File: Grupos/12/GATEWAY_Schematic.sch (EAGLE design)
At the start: 13 parts

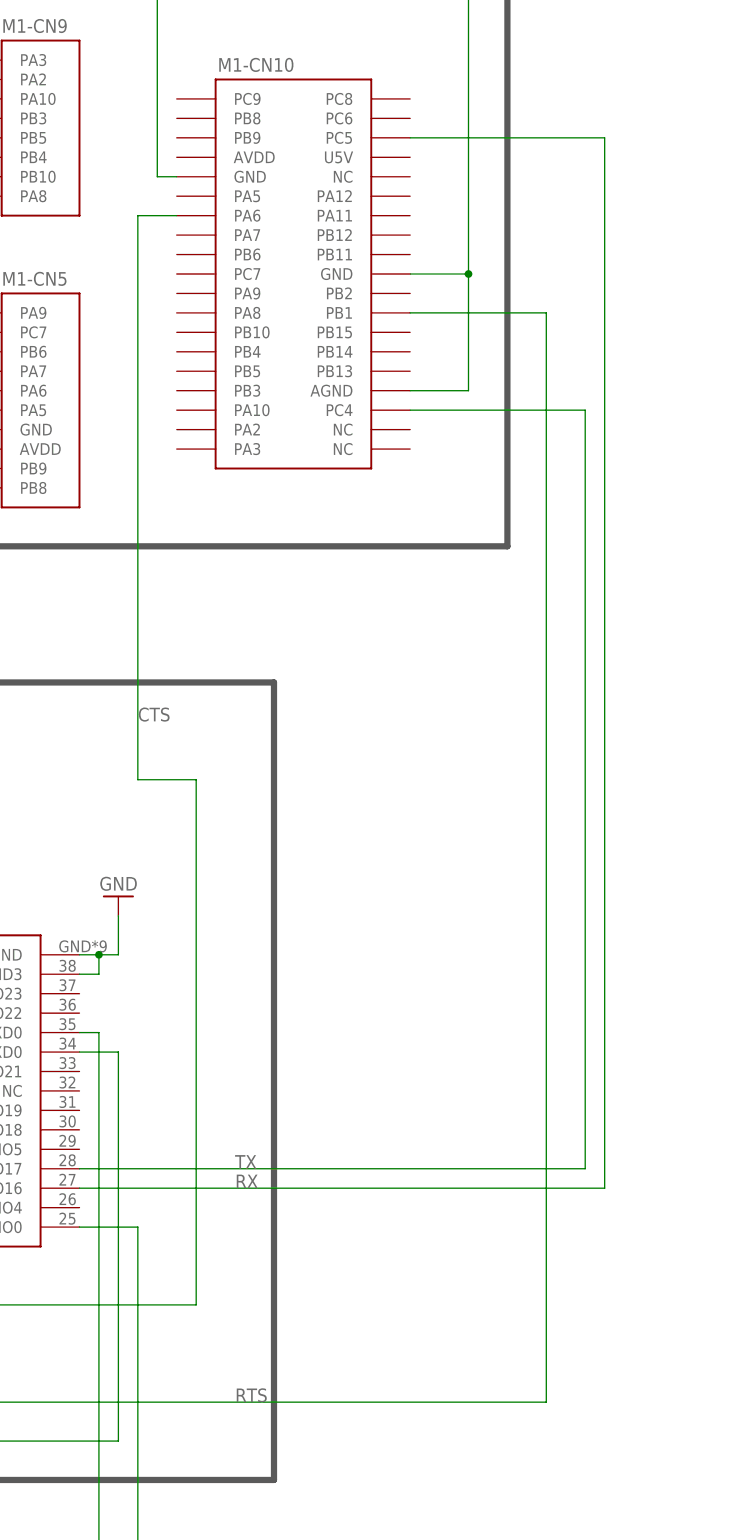
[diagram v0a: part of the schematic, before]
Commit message: Swap RTS/CTS and RX/TX
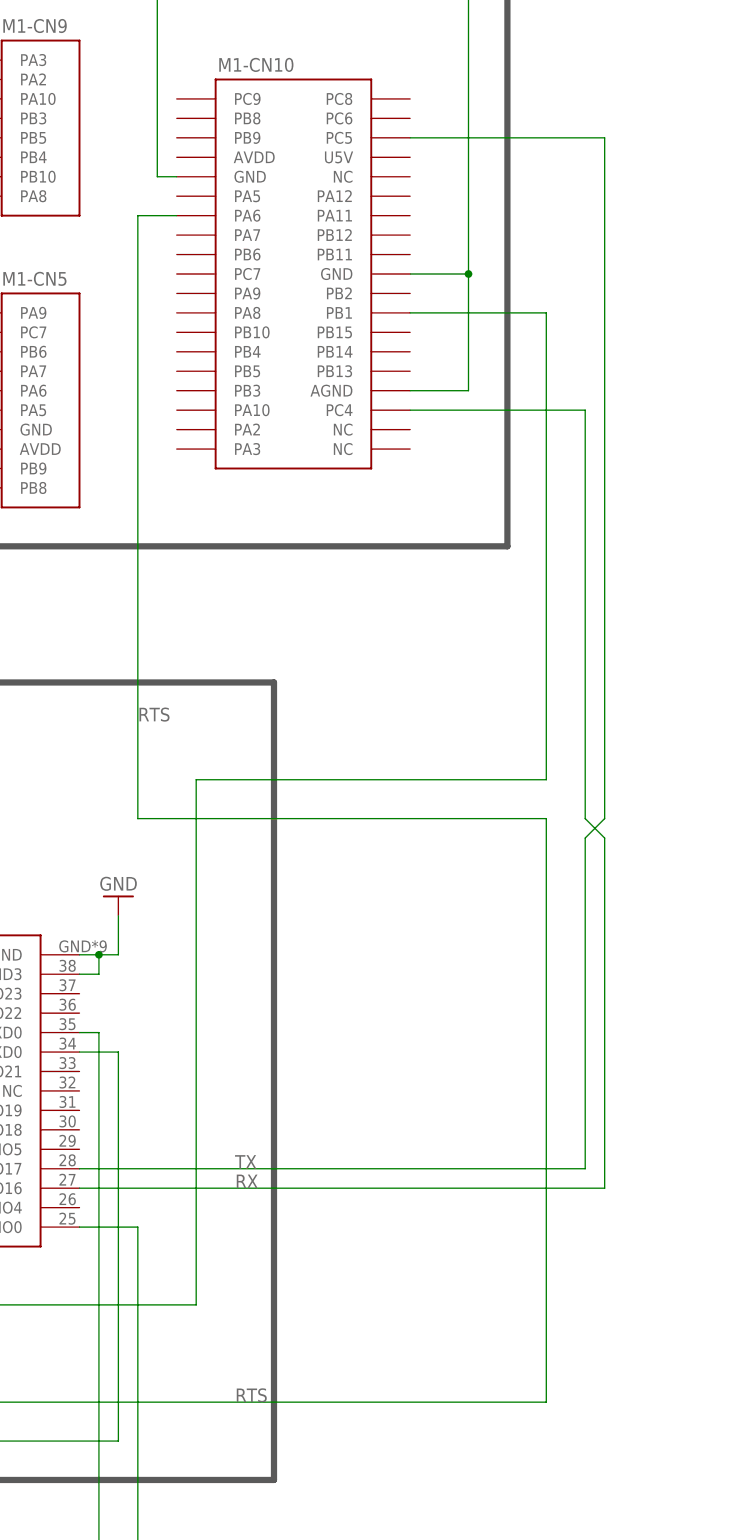
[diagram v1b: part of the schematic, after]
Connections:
- net CTS: now also M1-CN10.PB1; no longer M1-CN10.PA6
- net RTS: now also M1-CN10.PA6; no longer M1-CN10.PB1
- net RX: now also M1-CN10.PC4; no longer M1-CN10.PC5
- net TX: now also M1-CN10.PC5; no longer M1-CN10.PC4
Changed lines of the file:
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@@
 <drawing>
 <settings>
-<setting alwaysvectorfont="no"/>
+<setting alwaysvectorfont="yes"/>
 <setting verticaltext="up"/>
 </settings>
@@
 <net name="TX" class="0">
 <segment>
-<wire x1="66.04" y1="53.34" x2="88.9" y2="53.34" width="0.1524" layer="91"/>
-<wire x1="88.9" y1="53.34" x2="88.9" y2="-45.72" width="0.1524" layer="91"/>
 <wire x1="88.9" y1="-45.72" x2="22.86" y2="-45.72" width="0.1524" layer="91"/>
-<pinref part="M1" gate="-CN10" pin="PC4"/>
 <label x="43.18" y="-45.72" size="1.778" layer="95"/>
 <pinref part="ESP-WROOM-32" gate="G$1" pin="IO17"/>
+<wire x1="88.9" y1="-45.72" x2="88.9" y2="-2.54" width="0.1524" layer="91"/>
+<wire x1="88.9" y1="-2.54" x2="91.44" y2="0" width="0.1524" layer="91"/>
+<wire x1="66.04" y1="88.9" x2="91.44" y2="88.9" width="0.1524" layer="91"/>
+<pinref part="M1" gate="-CN10" pin="PC5"/>
+<wire x1="91.44" y1="0" x2="91.44" y2="88.9" width="0.1524" layer="91"/>
 </segment>
 </net>
 <net name="RX" class="0">
 <segment>
-<wire x1="66.04" y1="88.9" x2="91.44" y2="88.9" width="0.1524" layer="91"/>
-<wire x1="91.44" y1="88.9" x2="91.44" y2="-48.26" width="0.1524" layer="91"/>
 <wire x1="91.44" y1="-48.26" x2="22.86" y2="-48.26" width="0.1524" layer="91"/>
-<pinref part="M1" gate="-CN10" pin="PC5"/>
 <label x="43.18" y="-48.26" size="1.778" layer="95"/>
 <pinref part="ESP-WROOM-32" gate="G$1" pin="IO16"/>
+<wire x1="66.04" y1="53.34" x2="88.9" y2="53.34" width="0.1524" layer="91"/>
+<pinref part="M1" gate="-CN10" pin="PC4"/>
+<wire x1="88.9" y1="53.34" x2="88.9" y2="0" width="0.1524" layer="91"/>
+<wire x1="88.9" y1="0" x2="91.44" y2="-2.54" width="0.1524" layer="91"/>
+<wire x1="91.44" y1="-2.54" x2="91.44" y2="-48.26" width="0.1524" layer="91"/>
 </segment>
 </net>
@@
 <wire x1="38.1" y1="-63.5" x2="2.54" y2="-63.5" width="0.1524" layer="91"/>
 <wire x1="2.54" y1="-63.5" x2="2.54" y2="-60.96" width="0.1524" layer="91"/>
-<wire x1="38.1" y1="5.08" x2="30.48" y2="5.08" width="0.1524" layer="91"/>
-<wire x1="30.48" y1="5.08" x2="30.48" y2="78.74" width="0.1524" layer="91"/>
-<wire x1="30.48" y1="78.74" x2="35.56" y2="78.74" width="0.1524" layer="91"/>
-<pinref part="M1" gate="-CN10" pin="PA6"/>
-<label x="30.48" y="12.7" size="1.778" layer="95"/>
 <pinref part="ESP-WROOM-32" gate="G$1" pin="IO15"/>
+<wire x1="66.04" y1="66.04" x2="83.82" y2="66.04" width="0.1524" layer="91"/>
+<pinref part="M1" gate="-CN10" pin="PB1"/>
+<wire x1="38.1" y1="5.08" x2="83.82" y2="5.08" width="0.1524" layer="91"/>
+<wire x1="83.82" y1="5.08" x2="83.82" y2="66.04" width="0.1524" layer="91"/>
 </segment>
 </net>
 <net name="RTS" class="0">
 <segment>
-<wire x1="66.04" y1="66.04" x2="83.82" y2="66.04" width="0.1524" layer="91"/>
-<wire x1="83.82" y1="66.04" x2="83.82" y2="-76.2" width="0.1524" layer="91"/>
 <wire x1="83.82" y1="-76.2" x2="-38.1" y2="-76.2" width="0.1524" layer="91"/>
 <wire x1="-38.1" y1="-76.2" x2="-38.1" y2="-50.8" width="0.1524" layer="91"/>
 <wire x1="-38.1" y1="-50.8" x2="-35.56" y2="-50.8" width="0.1524" layer="91"/>
-<pinref part="M1" gate="-CN10" pin="PB1"/>
 <label x="43.18" y="-76.2" size="1.778" layer="95"/>
 <pinref part="ESP-WROOM-32" gate="G$1" pin="IO14"/>
-</segment>
-</net>
+<pinref part="M1" gate="-CN10" pin="PA6"/>
+<wire x1="30.48" y1="78.74" x2="35.56" y2="78.74" width="0.1524" layer="91"/>
+<wire x1="30.48" y1="0" x2="30.48" y2="78.74" width="0.1524" layer="91"/>
+<label x="30.48" y="12.7" size="1.778" layer="95"/>
+<wire x1="30.48" y1="0" x2="83.82" y2="0" width="0.1524" layer="91"/>
+<wire x1="83.82" y1="0" x2="83.82" y2="-76.2" width="0.1524" layer="91"/>
+</segment>
+</net>
